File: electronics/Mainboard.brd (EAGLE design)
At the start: 310 x 150 mm, 225 parts, among them J1 JST_PH_B3B-PH-K-S(LF)(SN), J10 JST_PH_B3B-PH-K-S(LF)(SN), J11 JST_PH_B3B-PH-K-S(LF)(SN), J12 JST_PH_B3B-PH-K-S(LF)(SN), J13 JST_PH_B3B-PH-K-S(LF)(SN), J14 JST_PH_B3B-PH-K-S(LF)(SN), J15 JST_PH_B3B-PH-K-S(LF)(SN), J16 JST_PH_B3B-PH-K-S(LF)(SN), J17 JST_PH_B3B-PH-K-S(LF)(SN), J18 JST_PH_B3B-PH-K-S(LF)(SN), J19 JST_PH_B3B-PH-K-S(LF)(SN), J2 JST_PH_B3B-PH-K-S(LF)(SN), J20 JST_PH_B3B-PH-K-S(LF)(SN), J21 JST_PH_B3B-PH-K-S(LF)(SN), J22 JST_PH_B3B-PH-K-S(LF)(SN), J23 JST_PH_B3B-PH-K-S(LF)(SN), J24 JST_PH_B3B-PH-K-S(LF)(SN), J25 JST_PH_B3B-PH-K-S(LF)(SN), J26 JST_PH_B3B-PH-K-S(LF)(SN), J27 JST_PH_B3B-PH-K-S(LF)(SN), J28 JST_PH_B3B-PH-K-S(LF)(SN), J29 JST_PH_B3B-PH-K-S(LF)(SN), J3 JST_PH_B3B-PH-K-S(LF)(SN), J30 JST_PH_B3B-PH-K-S(LF)(SN), J31 JST_PH_B3B-PH-K-S(LF)(SN), J32 JST_PH_B3B-PH-K-S(LF)(SN), J4 JST_PH_B3B-PH-K-S(LF)(SN), J5 JST_PH_B3B-PH-K-S(LF)(SN), J6 JST_PH_B3B-PH-K-S(LF)(SN), J7 JST_PH_B3B-PH-K-S(LF)(SN), J8 JST_PH_B3B-PH-K-S(LF)(SN), J9 JST_PH_B3B-PH-K-S(LF)(SN), U15 AD5360BSTZ, U16 ADR425ARZ, U18 AD7730BRUZ, U19 AD5360BSTZ, U20 ADR425ARZ, U21 AD7730BRUZ, U22 STM32F103RCT6, U23 AD7730BRUZ, U24 AD7730BRUZ, U25 AD7730BRUZ, U26 AD7730BRUZ, U27 AD7730BRUZ, U28 AD7730BRUZ, U38 AD7730BRUZ, U39 AD7730BRUZ, U4 ADR421ARZ, U40 STM32F103RCT6, U41 AD7730BRUZ, U42 AD7730BRUZ, U43 AD7730BRUZ, U44 AD7730BRUZ, U45 AD7730BRUZ, U46 AD7730BRUZ, U5 AD7616BSTZ, U6 74AHC1G04GW/T1, U7 ADR421ARZ, U8 AD7616BSTZ, U9 74AHC1G04GW/T1, X1 22-23-2031, Y3 KC2520B-C1, Y4 ABM3B, Y7 KC2520B-C1, Y8 ABM3B

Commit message: finished layout
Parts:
- moved C137 3.68 mm to (150.2, 112.5), turned to 45 degrees
- moved C103 3.68 mm to (150.2, 35.1), turned to 45 degrees
- moved C21 3.25 mm to (144.3, 119.0), turned to 45 degrees
- moved C1 2.76 mm to (144.3, 41.6), turned to 45 degrees
- moved C47 2.00 mm to (48.5, 123.5)
- moved C78 2.00 mm to (48.5, 45.5)
- moved R15 1.95 mm to (118.3, 37.7)
- moved R16 1.95 mm to (118.3, 40.3)
- moved R19 1.95 mm to (118.3, 114.4)
- moved R20 1.95 mm to (118.3, 117.0)
- moved C46 1.95 mm to (50.7, 123.5)
- moved C77 1.95 mm to (50.7, 45.5)
- moved S3 1.95 mm to (66.3, 48.1)
- moved C102 1.95 mm to (145.6, 39.0), turned to 45 degrees
- moved C2 1.45 mm to (152.8, 33.8), turned to 45 degrees
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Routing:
- net VDD: track 984.6 -> 1027.7 mm
- net VSS: track 443.2 -> 484.6 mm
- net N$39: track 16.7 -> 24.6 mm, vias 0 -> 1
- net N$75: track 18.7 -> 24.6 mm, vias 0 -> 1
- net DVCC: track 1560.7 -> 1566.5 mm
- net MISO: track 680.2 -> 675.8 mm
- net MOSI: track 683.8 -> 680.5 mm
- net N$152: track 50.5 -> 47.2 mm
- net SCLK: track 660.0 -> 656.7 mm
- net N$220: track 50.2 -> 47.6 mm
- net N$151: track 24.2 -> 22.3 mm
- net N$219: track 24.0 -> 22.0 mm
- net SS_DAC_1: track 180.9 -> 179.9 mm
- net ADC_1_VREF: track 14.2 -> 13.3 mm
- net SS_DAC_2: track 121.6 -> 121.0 mm

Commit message: added missing trace names
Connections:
- net N$151 renamed DAC_1_CLR
- net N$152 renamed DAC_1_RST
- net N$2 renamed PG_CURR_LIM
- net N$219 renamed DAC_2_CLR
- net N$220 renamed DAC_2_RST
- net N$3 renamed DVCC_CURR_LIM
- net N$37 renamed ADC_2_REFCAP
- net N$38 renamed ADC_2_COM_MODE
- net N$39 renamed ADC_2_RST
- net N$4 renamed +5V_CURR_LIM
- net N$40 renamed ADC_2_REFINOUT
- net N$5 renamed VDD_CURR_LIM
- net N$6 renamed HB_CURR_LIM
- net N$63 renamed ADC_2_REGCAP
- net N$64 renamed ADC_2_REGCAPD
- net N$73 renamed ADC_1_REFCAP
- net N$74 renamed ADC_1_COM_MODE
- net N$75 renamed ADC_1_RST
- net N$76 renamed ADC_1_REFINOUT
- net N$86 renamed ADC_1_REGCAP
- net N$87 renamed ADC_1_REGCAPD
- net ADC_1_VREF: now also C30.+, C66.1, C67.1, R9.2, U7.6; no longer C28.+, C35.1, C36.1, R6.2, U4.6
- net ADC_2_VREF: now also C28.+, C35.1, C36.1, R6.2, U4.6; no longer C30.+, C66.1, C67.1, R9.2, U7.6

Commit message: minor changes on names and routing
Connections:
- net N$1 renamed RPI_PWR
- net N$41 renamed ADC_2_CONVST
- net N$77 renamed ADC_1_CONVST
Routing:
- net LC_1_SPI1_MISO: track 125.6 -> 124.7 mm
- net LC_2_SPI1_MISO: track 125.4 -> 124.5 mm
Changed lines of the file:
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@@
 <contactref element="U27" pad="21"/>
 <contactref element="U28" pad="21"/>
-<wire x1="213.2" y1="100.75" x2="224.9" y2="100.75" width="0.254" layer="16"/>
-<wire x1="224.9" y1="100.75" x2="236.6" y2="100.75" width="0.254" layer="16"/>
-<via x="224.9" y="100.75" extent="1-16" drill="0.3048"/>
+<wire x1="213.2" y1="100.75" x2="224.25" y2="100.75" width="0.254" layer="16"/>
+<wire x1="224.25" y1="100.75" x2="236.6" y2="100.75" width="0.254" layer="16"/>
+<via x="224.25" y="100.75" extent="1-16" drill="0.3048"/>
 <wire x1="236.6" y1="100.75" x2="248.3" y2="100.75" width="0.254" layer="16"/>
 <wire x1="248.3" y1="100.75" x2="260" y2="100.75" width="0.254" layer="16"/>
@@
 <wire x1="223.075" y1="100.875" x2="223.2" y2="100.75" width="0.254" layer="1"/>
 <wire x1="223.075" y1="100.875" x2="223.2" y2="100.75" width="0.254" layer="1"/>
-<wire x1="223.2" y1="100.75" x2="224.9" y2="100.75" width="0.254" layer="1"/>
+<wire x1="223.2" y1="100.75" x2="224.25" y2="100.75" width="0.254" layer="1"/>
 <wire x1="233.5694" y1="101.074996875" x2="234.575003125" y2="101.074996875" width="0.254" layer="1"/>
 <wire x1="234.575003125" y1="101.074996875" x2="234.9" y2="100.75" width="0.254" layer="1"/>
@@
 <wire x1="224.25" y1="109.85" x2="224.25" y2="106.25" width="0.254" layer="16"/>
 <via x="224.25" y="106.25" extent="1-16" drill="0.3048"/>
-<wire x1="224.9" y1="102.7" x2="224.9" y2="100.75" width="0.254" layer="1"/>
-<wire x1="224.25" y1="103.35" x2="224.9" y2="102.7" width="0.254" layer="1"/>
-<wire x1="224.25" y1="106.25" x2="224.25" y2="103.35" width="0.254" layer="1"/>
+<wire x1="224.25" y1="106.25" x2="224.25" y2="100.75" width="0.254" layer="1"/>
 </signal>
 <signal name="LC_1_SPI1_MOSI">
@@
 <wire x1="211.9" y1="101.75" x2="216.45" y2="101.75" width="0.254" layer="16"/>
 <wire x1="216.45" y1="101.75" x2="223.6" y2="101.75" width="0.254" layer="16"/>
-<wire x1="223.6" y1="101.75" x2="225.55" y2="101.75" width="0.254" layer="16"/>
-<wire x1="225.55" y1="101.75" x2="235.3" y2="101.75" width="0.254" layer="16"/>
+<wire x1="223.6" y1="101.75" x2="225.35" y2="101.75" width="0.254" layer="16"/>
+<wire x1="225.35" y1="101.75" x2="235.3" y2="101.75" width="0.254" layer="16"/>
 <wire x1="235.3" y1="101.75" x2="247" y2="101.75" width="0.254" layer="16"/>
 <wire x1="247" y1="101.75" x2="258.7" y2="101.75" width="0.254" layer="16"/>
@@
 <via x="225.35" y="109.85" extent="1-16" drill="0.3048"/>
 <via x="225.35" y="106.25" extent="1-16" drill="0.3048"/>
-<via x="225.55" y="101.75" extent="1-16" drill="0.3048"/>
+<via x="225.35" y="101.75" extent="1-16" drill="0.3048"/>
 <wire x1="224.138" y1="115.162" x2="225.35" y2="113.95" width="0.254" layer="1"/>
-<wire x1="225.55" y1="104.5747375" x2="225.55" y2="101.75" width="0.254" layer="1"/>
-<wire x1="225.35" y1="106.25" x2="225.35" y2="104.7747375" width="0.254" layer="1"/>
-<wire x1="225.35" y1="104.7747375" x2="225.55" y2="104.5747375" width="0.254" layer="1"/>
+<wire x1="225.35" y1="106.25" x2="225.35" y2="105.3" width="0.254" layer="1"/>
+<wire x1="225.35" y1="105.3" x2="225.35" y2="104.7747375" width="0.254" layer="1"/>
 <wire x1="225.35" y1="109.85" x2="225.35" y2="106.25" width="0.254" layer="16"/>
+<wire x1="225.35" y1="101.75" x2="225.35" y2="105.3" width="0.254" layer="1"/>
 </signal>
 <signal name="BT_1_MCLK_OUT">
@@
 <contactref element="U45" pad="21"/>
 <contactref element="U46" pad="21"/>
-<wire x1="213.2" y1="24.05" x2="224.9" y2="24.05" width="0.254" layer="16"/>
-<wire x1="224.9" y1="24.05" x2="236.6" y2="24.05" width="0.254" layer="16"/>
+<wire x1="213.2" y1="24.05" x2="224.25" y2="24.05" width="0.254" layer="16"/>
+<wire x1="224.25" y1="24.05" x2="236.6" y2="24.05" width="0.254" layer="16"/>
 <wire x1="236.6" y1="24.05" x2="248.3" y2="24.05" width="0.254" layer="16"/>
 <wire x1="248.3" y1="24.05" x2="260" y2="24.05" width="0.254" layer="16"/>
@@
 <wire x1="221.8694" y1="24.374996875" x2="222.625003125" y2="24.374996875" width="0.254" layer="1"/>
 <wire x1="222.625003125" y1="24.374996875" x2="222.95" y2="24.05" width="0.254" layer="1"/>
-<wire x1="222.95" y1="24.05" x2="224.9" y2="24.05" width="0.254" layer="1"/>
-<via x="224.9" y="24.05" extent="1-16" drill="0.3048"/>
+<wire x1="222.95" y1="24.05" x2="224.25" y2="24.05" width="0.254" layer="1"/>
+<via x="224.25" y="24.05" extent="1-16" drill="0.3048"/>
 <wire x1="233.5694" y1="24.374996875" x2="234.325003125" y2="24.374996875" width="0.254" layer="1"/>
 <wire x1="234.325003125" y1="24.374996875" x2="234.65" y2="24.05" width="0.254" layer="1"/>
@@
 <wire x1="224.25" y1="33.15" x2="224.25" y2="29.25" width="0.254" layer="16"/>
 <via x="224.25" y="29.25" extent="1-16" drill="0.3048"/>
-<wire x1="224.25" y1="29.25" x2="224.25" y2="26.65" width="0.254" layer="1"/>
-<wire x1="224.25" y1="26.65" x2="224.9" y2="26" width="0.254" layer="1"/>
-<wire x1="224.9" y1="26" x2="224.9" y2="24.05" width="0.254" layer="1"/>
+<wire x1="224.25" y1="29.25" x2="224.25" y2="24.05" width="0.254" layer="1"/>
 </signal>
 <signal name="LC_2_SPI1_MOSI">
@@
 <wire x1="211.9" y1="25.05" x2="216.45" y2="25.05" width="0.254" layer="16"/>
 <wire x1="216.45" y1="25.05" x2="223.6" y2="25.05" width="0.254" layer="16"/>
-<wire x1="223.6" y1="25.05" x2="225.55" y2="25.05" width="0.254" layer="16"/>
-<wire x1="225.55" y1="25.05" x2="228.15" y2="25.05" width="0.254" layer="16"/>
+<wire x1="223.6" y1="25.05" x2="225.35" y2="25.05" width="0.254" layer="16"/>
+<wire x1="225.35" y1="25.05" x2="228.15" y2="25.05" width="0.254" layer="16"/>
 <wire x1="228.15" y1="25.05" x2="235.3" y2="25.05" width="0.254" layer="16"/>
 <wire x1="235.3" y1="25.05" x2="247" y2="25.05" width="0.254" layer="16"/>
@@
 <wire x1="225.35" y1="29.2636" x2="225.3364" y2="29.25" width="0.254" layer="16"/>
 <via x="225.3364" y="29.25" extent="1-16" drill="0.3048"/>
-<via x="225.55" y="25.05" extent="1-16" drill="0.3048"/>
-<wire x1="225.3364" y1="29.25" x2="225.3364" y2="28.1636" width="0.254" layer="1"/>
-<wire x1="225.3364" y1="28.1636" x2="225.55" y2="27.95" width="0.254" layer="1"/>
-<wire x1="225.55" y1="27.95" x2="225.55" y2="25.05" width="0.254" layer="1"/>
+<via x="225.35" y="25.05" extent="1-16" drill="0.3048"/>
+<wire x1="225.3364" y1="25.0636" x2="225.35" y2="25.05" width="0.254" layer="1"/>
+<wire x1="225.3364" y1="29.25" x2="225.3364" y2="25.0636" width="0.254" layer="1"/>
 </signal>
 <signal name="BT2_1_MCLK_OUT">
@@
 <wire x1="61.1" y1="115.7" x2="64.0394" y2="118.6394" width="0.4064" layer="16"/>
 </signal>
-<signal name="N$41">
+<signal name="ADC_2_CONVST">
 <contactref element="U5" pad="68"/>
 <contactref element="U6" pad="4"/>
@@
 <wire x1="26.4" y1="105.5" x2="28" y2="105.5" width="0.4064" layer="1"/>
 </signal>
-<signal name="N$77">
+<signal name="ADC_1_CONVST">
 <contactref element="U8" pad="68"/>
 <contactref element="U9" pad="4"/>
@@
 <wire x1="291.85" y1="120.28" x2="291.85" y2="97.8" width="0.4064" layer="1"/>
 </signal>
-<signal name="N$1">
+<signal name="RPI_PWR">
 <contactref element="SV1" pad="4"/>
 <contactref element="SV1" pad="2"/>

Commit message: minor re-routing
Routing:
- net ADC2_3: track 32.0 -> 35.5 mm
- net ADC1_3: track 31.8 -> 35.1 mm
- net ADC2_11: track 27.9 -> 27.0 mm
- net ADC1_11: track 27.2 -> 26.4 mm
- net ADC2_2: track 38.4 -> 39.2 mm
- net ADC1_5: track 24.3 -> 23.6 mm
- net ADC2_10: track 31.3 -> 30.7 mm
- net ADC1_10: track 30.7 -> 30.1 mm

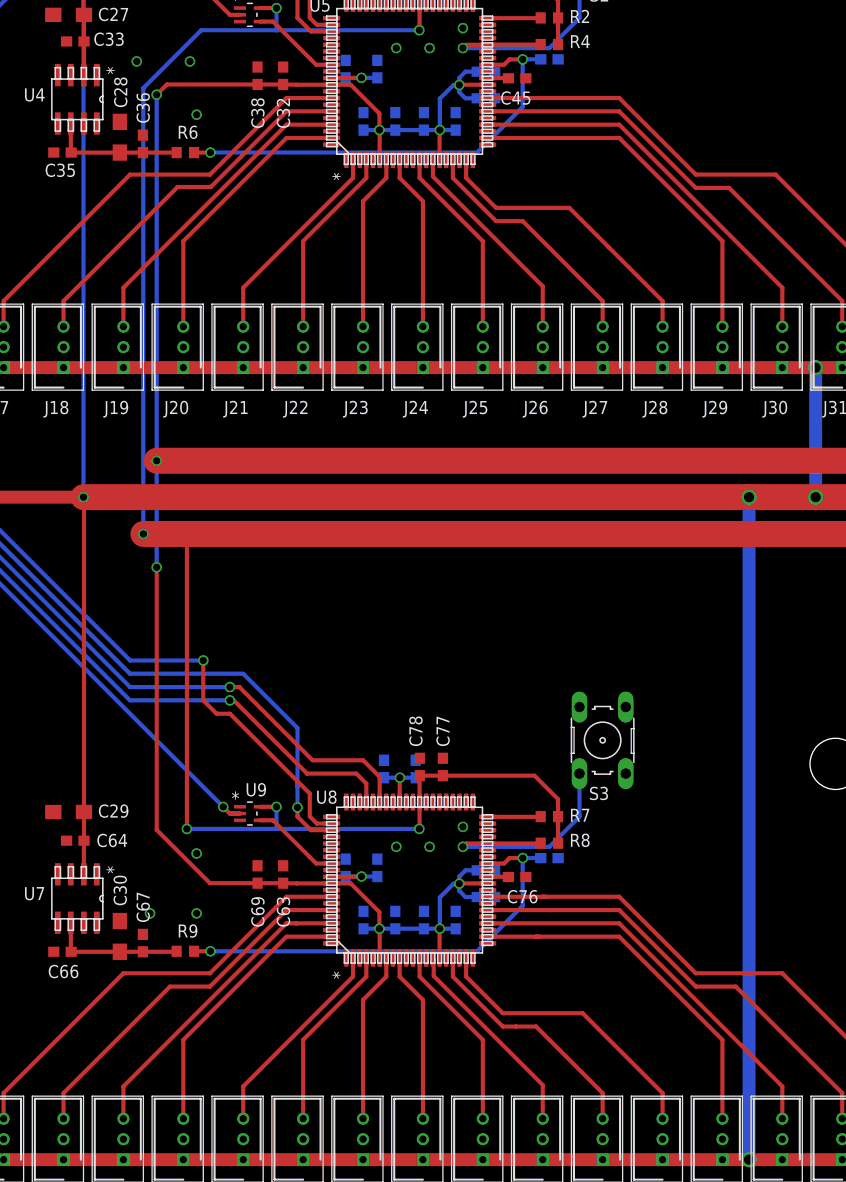
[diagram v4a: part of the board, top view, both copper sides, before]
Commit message: minor re-routing around the ADCs to spread ground plane further
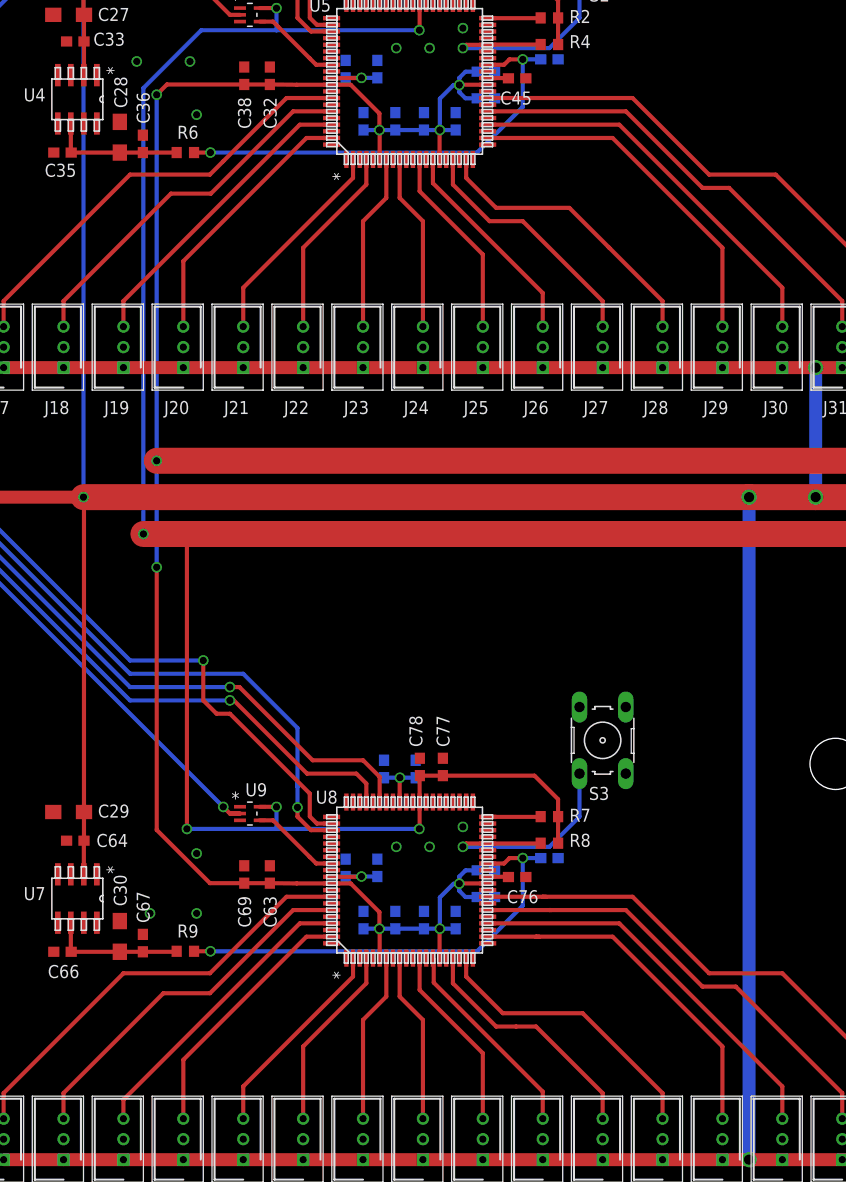
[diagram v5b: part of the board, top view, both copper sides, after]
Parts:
- moved C32 1.30 mm to (33.8, 113.0)
- moved C63 1.30 mm to (33.8, 35.0)
- moved C38 1.30 mm to (31.3, 113.0)
- moved C69 1.30 mm to (31.3, 35.0)
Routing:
- net ADC1_11: track 26.4 -> 25.2 mm
- net ADC2_11: track 27.0 -> 25.9 mm
- net ADC1_10: track 30.1 -> 29.3 mm
- net ADC2_10: track 30.7 -> 30.0 mm
